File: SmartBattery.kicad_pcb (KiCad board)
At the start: 2 copper layers, 102 parts, among them J1 USB_C_Receptacle_USB2.0, J10 Conn_01x02, J11 Conn_01x02, J2 ST-USB-003A, J3 RJ45_LED_Shielded, J4 Conn_01x02, J5 Conn_01x02, J6 Conn_01x02, J7 Conn_01x02, J8 Conn_01x02, J9 Conn_01x02, Q1 2n7002K, Q2 AO4468, Q3 AO4468, Q4 AO4468, Q5 AO4468, Q6 2n7002K, SW1 SW_Push, SW2 SW_Push, U101 BQ2947xx, U102 BQ40Z50

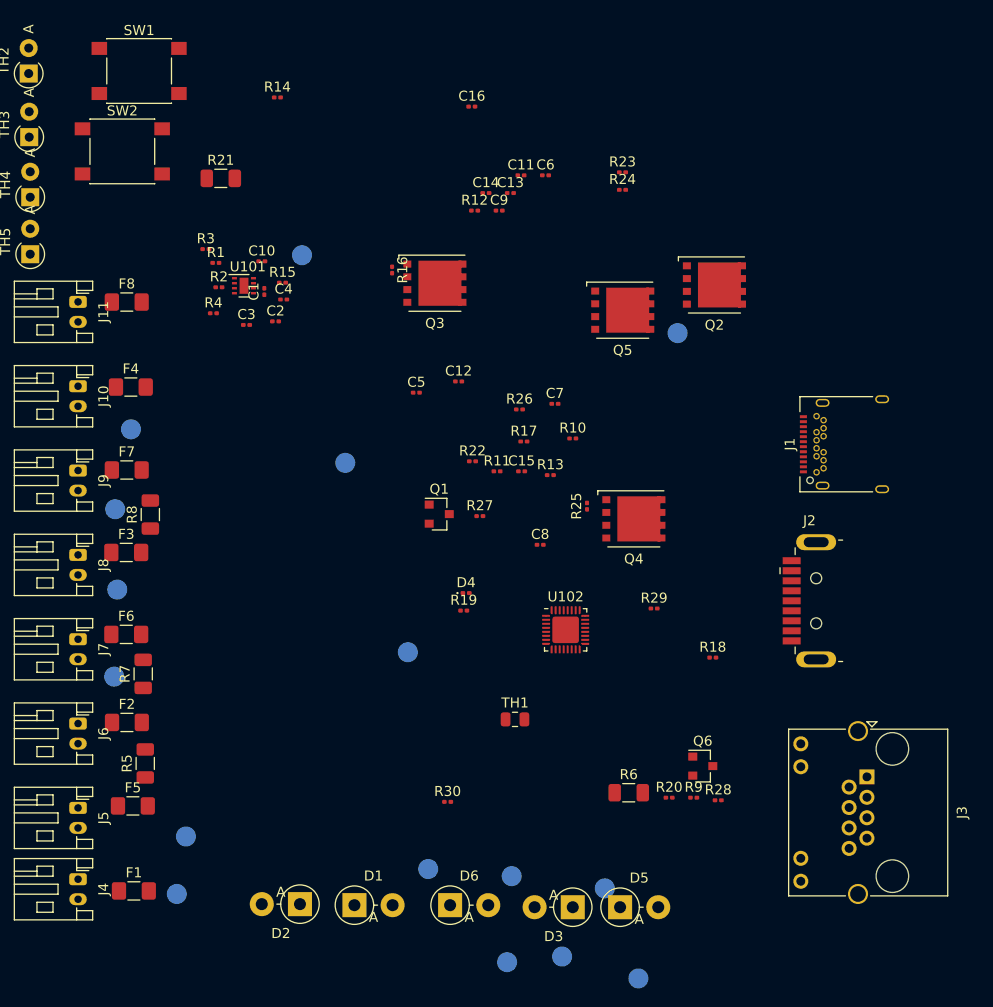
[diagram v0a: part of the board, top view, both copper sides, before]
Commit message: Added capacitors, inductors to charger page. Fixed capacitor sizes.
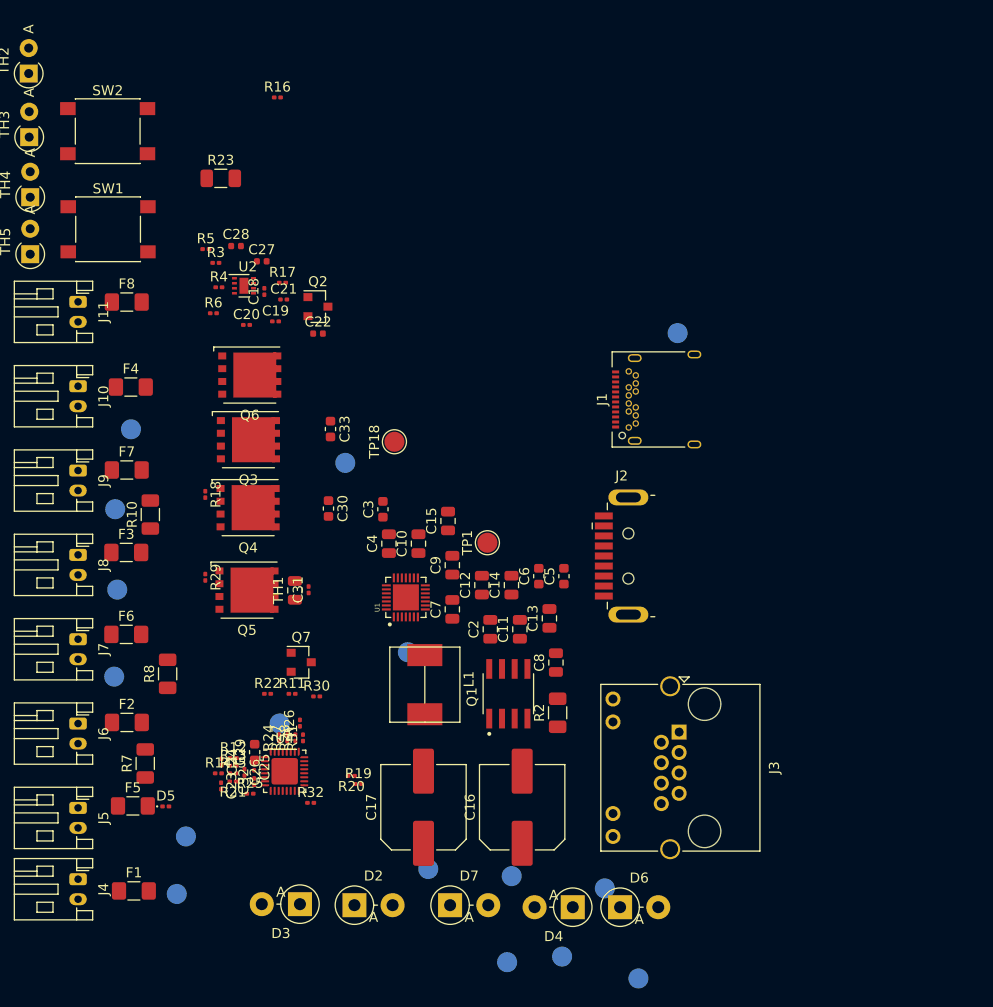
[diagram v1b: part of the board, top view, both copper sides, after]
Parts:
- removed the R7 at (66.0, 108.5)
- added C10: 10u, Capacitor_SMD:C_0805_2012Metric, F.Cu at (93.5, 95.5)
- added C11: 10u, Capacitor_SMD:C_0805_2012Metric, F.Cu at (103.6, 104.1)
- added C12: 22u, Capacitor_SMD:C_0805_2012Metric, F.Cu at (99.8, 99.7)
- added C13: 22u, Capacitor_SMD:C_0805_2012Metric, F.Cu at (106.5, 103.0)
- added C14: 22u, Capacitor_SMD:C_0805_2012Metric, F.Cu at (102.7, 99.7)
- added C15: 22u, Capacitor_SMD:C_0805_2012Metric, F.Cu at (96.4, 93.3)
- added C16: 220u, Capacitor_SMD:C_Elec_8x10.2, F.Cu at (103.8, 121.8)
- added C17: 220u, Capacitor_SMD:C_Elec_8x10.2, F.Cu at (94.0, 121.8)
- added C2: 10u, Capacitor_SMD:C_0805_2012Metric, F.Cu at (100.6, 104.1)
- added C3: 0.1u, Capacitor_SMD:C_0603_1608Metric, F.Cu at (89.9, 92.1)
- added C4: 22u, Capacitor_SMD:C_0805_2012Metric, F.Cu at (90.5, 95.5)
- added C5: 0.1u, Capacitor_SMD:C_0603_1608Metric, F.Cu at (108.0, 98.8)
- added C6: 0.1u, Capacitor_SMD:C_0603_1608Metric, F.Cu at (105.5, 98.8)
- added C7: 22u, Capacitor_SMD:C_0805_2012Metric, F.Cu at (96.8, 102.1)
- added C8: 10u, Capacitor_SMD:C_0805_2012Metric, F.Cu at (107.2, 107.4)
- added C9: 22u, Capacitor_SMD:C_0805_2012Metric, F.Cu at (96.8, 97.7)
- added L1: MWSA0603-2R2MT, SmartBattery:MWSA0603, F.Cu at (92.2, 111.5)
- added Q2: 2n7002K, Package_TO_SOT_SMD:SOT-23, F.Cu at (83.4, 71.9)
- added R2: 0.01, Resistor_SMD:R_1206_3216Metric, F.Cu at (107.4, 112.4)
- added TP1: TestPoint, TestPoint:TestPoint_Pad_D2.0mm, F.Cu at (100.3, 95.4)
- added TP18: TestPoint, TestPoint:TestPoint_Pad_D2.0mm, F.Cu at (91.1, 85.4)
- added U1: bq2477x, SmartBattery:QFN40P400X400X80-29N, F.Cu at (92.2, 100.9)
- C18: renamed from C1; value C -> 0.1u 6.3v
- C19: renamed from C2; value C -> 0.1u 6.3v
- C20: renamed from C3; value C -> 0.1u 6.3v
- C21: renamed from C4; value C -> 0.1u 6.3v
- C22: renamed from C5; value 0.1uF -> 0.1uF 25v; footprint Capacitor_SMD:C_0201_0603Metric -> Capacitor_SMD:C_0402_1005Metric
- C23: renamed from C6; value C -> 0.1u 6.3v
- C24: renamed from C7; value C -> 0.1u 6.3v
- C25: renamed from C8; value C -> 0.1u 6.3v
- C26: renamed from C9; value C -> 0.1u 6.3v
- C27: renamed from C10; value C -> 0.1u 20v; footprint Capacitor_SMD:C_0201_0603Metric -> Capacitor_SMD:C_0402_1005Metric
- C28: renamed from C11; value C -> 0.1u 20v; footprint Capacitor_SMD:C_0201_0603Metric -> Capacitor_SMD:C_0402_1005Metric
- C29: renamed from C12; value 2.2u -> 2.2u 50v; footprint Capacitor_SMD:C_0201_0603Metric -> Capacitor_SMD:C_0603_1608Metric
- C30: renamed from C13; footprint Capacitor_SMD:C_0201_0603Metric -> Capacitor_SMD:C_0603_1608Metric
- C32: renamed from C15; value 0.1u -> 0.1u 6.3v
- C33: renamed from C16; footprint Capacitor_SMD:C_0201_0603Metric -> Capacitor_SMD:C_0603_1608Metric
- Q1: value 2n7002K -> AO4407A; footprint Package_TO_SOT_SMD:SOT-23 -> SmartBattery:SOIC127P600X175-8N
- U2: renamed from U101; value BQ2947xx -> BQ294706DSGR
- moved R25 72.3 mm to (76.7, 120.5)
- moved C23 69.0 mm to (73.8, 119.7), turned to 270 degrees
- moved R26 62.2 mm to (81.6, 113.5), turned to 90 degrees
- moved R14 61.7 mm to (73.5, 118.5)
- moved C26 61.6 mm to (76.1, 118.4), turned to 270 degrees
- moved Q3 49.0 mm to (76.5, 85.2)
- moved C24 48.8 mm to (73.8, 117.3), turned to 270 degrees
- moved R8 47.5 mm to (68.4, 108.5), turned to 90 degrees
- moved TP13 46.8 mm to (79.6, 113.5)
- moved R12 46.5 mm to (75.0, 116.9)
- moved R15 43.5 mm to (75.0, 118.5)
- moved C31 43.4 mm to (82.5, 100.1), turned to 90 degrees
- moved C29 42.2 mm to (77.1, 116.3), turned to 90 degrees
- moved R22 41.4 mm to (78.4, 110.5)
- moved Q7 41.4 mm to (81.8, 107.4)
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- renumbered C14 to C31, D1 to D2, D2 to D3, D3 to D4, D4 to D5, D5 to D6, D6 to D7, Q2 to Q3, Q3 to Q4, Q4 to Q5, Q5 to Q6, Q6 to Q7, R8 to R10, R9 to R11, R10 to R12, R11 to R13, R12 to R14, R13 to R15, R14 to R16, R15 to R17, R16 to R18, R17 to R19, R18 to R20, R19 to R21, R20 to R22, R21 to R23, R22 to R24, R23 to R25, R24 to R26, R25 to R27, R26 to R28, R27 to R29, R1 to R3, R28 to R30, R29 to R31, R30 to R32, R2 to R4, R3 to R5, R4 to R6, R5 to R7, R6 to R8, TP17 to TP10, TP18 to TP11, TP19 to TP12, TP20 to TP13, TP21 to TP14, TP22 to TP15, TP23 to TP16, TP24 to TP17, TP9 to TP2, TP10 to TP3, TP11 to TP4, TP12 to TP5, TP13 to TP6, TP14 to TP7, TP15 to TP8, TP16 to TP9, U102 to U4
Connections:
- net BATT_SHUTDOWN renamed /Battery connection and protection/BATT_SHUTDOWN_N
- net BTP_INT renamed /Battery connection and protection/BATT_INT
- net PACK_+ renamed /Battery connection and protection/BATT_PACK_P
- net SMB_C renamed /Battery connection and protection/BATT_SMB_C
- net SMB_D renamed /Battery connection and protection/BATT_SMB_D
- Q1 pad 1: FUSE_HEATER -> Net-(C10-Pad1)
- Q1 pad 2: BAT_VN_0 -> Net-(C10-Pad1)
- Q1 pad 3: Net-(Q1-Pad3) -> Net-(C10-Pad1)
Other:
- net class Default: clearance 0.2 -> 0.18; trace_width 0.25 -> 0.18; via_dia 0.8 -> 0.4; via_drill 0.4 -> 0.3
- rule trace_clearance: 0.2 -> 0.18
- rule trace_min: 0.2 -> 0.16

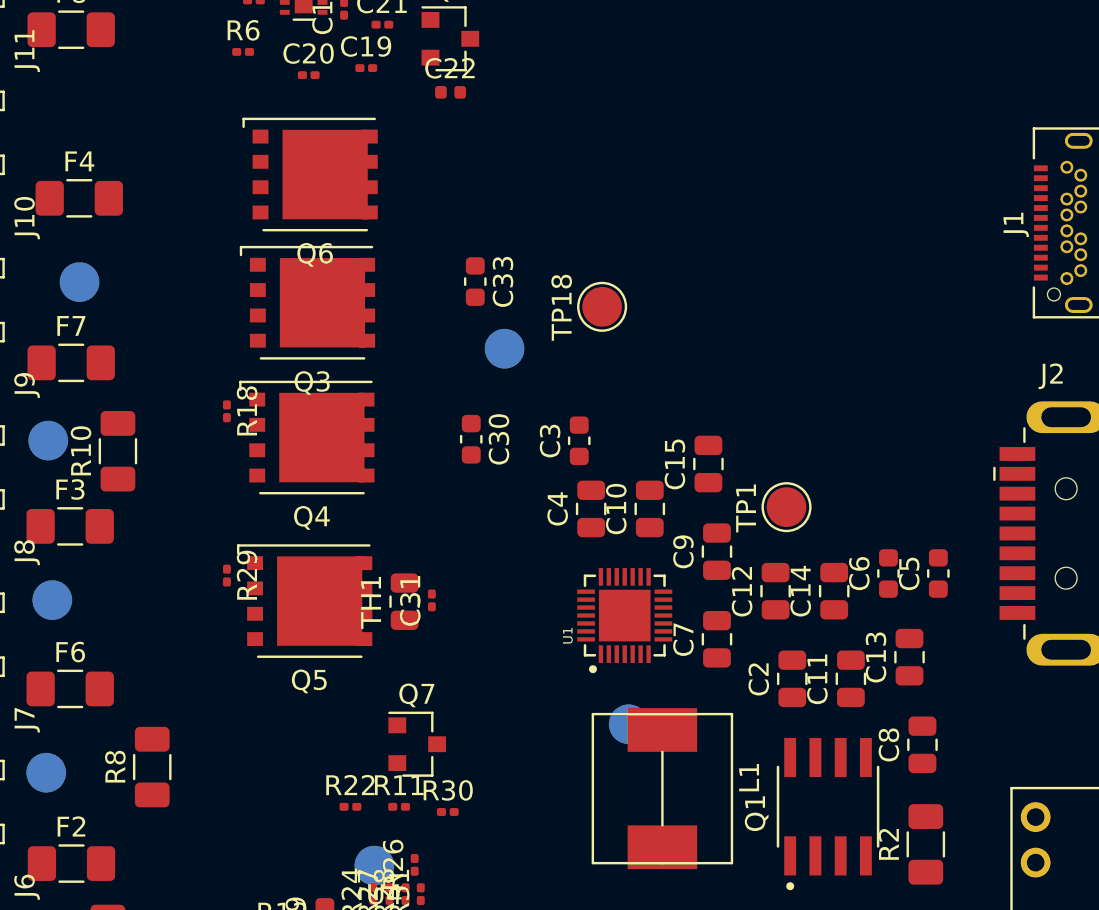
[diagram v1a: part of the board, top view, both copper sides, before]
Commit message: Added bunch of cap to charger, made footprint for diode + fuse
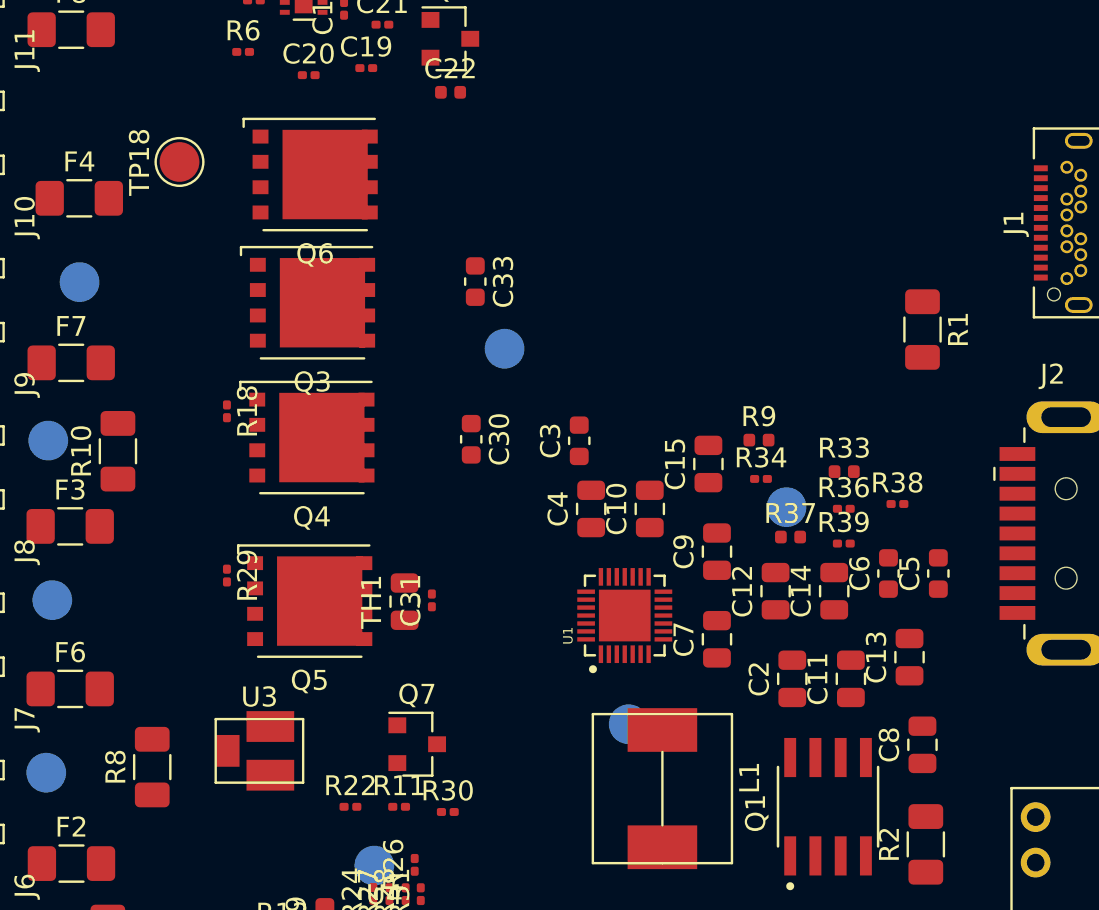
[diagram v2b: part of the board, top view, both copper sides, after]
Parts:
- added R1: 0.01, Resistor_SMD:R_1206_3216Metric, F.Cu at (107.2, 86.5)
- added R33: 2, Resistor_SMD:R_0402_1005Metric, F.Cu at (103.2, 93.7)
- added R34: 10M, Resistor_SMD:R_0201_0603Metric, F.Cu at (99.1, 94.0)
- added R36: 0, Resistor_SMD:R_0201_0603Metric, F.Cu at (103.2, 95.5)
- added R37: 15, Resistor_SMD:R_0402_1005Metric, F.Cu at (100.5, 97.0)
- added R38: 0, Resistor_SMD:R_0201_0603Metric, F.Cu at (105.9, 95.3)
- added R39: 1M, Resistor_SMD:R_0201_0603Metric, F.Cu at (103.2, 97.3)
- added R9: 10M, Resistor_SMD:R_0402_1005Metric, F.Cu at (99.0, 92.1)
- added U3: ITV4030, SmartBattery:ITV4030, F.Cu at (73.8, 107.7)
- TP1: moved to B.Cu
- moved TP18 22.5 mm to (69.8, 78.1)
- turned TP1 to 270 degrees
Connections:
- net Net-(U1-Pad7) renamed /Charger/IADP
- net Net-(U1-Pad8) renamed /Charger/IBAT
- U1 pad 22: Net-(U1-Pad22) -> GND
- U1 pad 29: Net-(U1-Pad29) -> GND
- U1 pad 9: Net-(U1-Pad9) -> /Charger/PMON

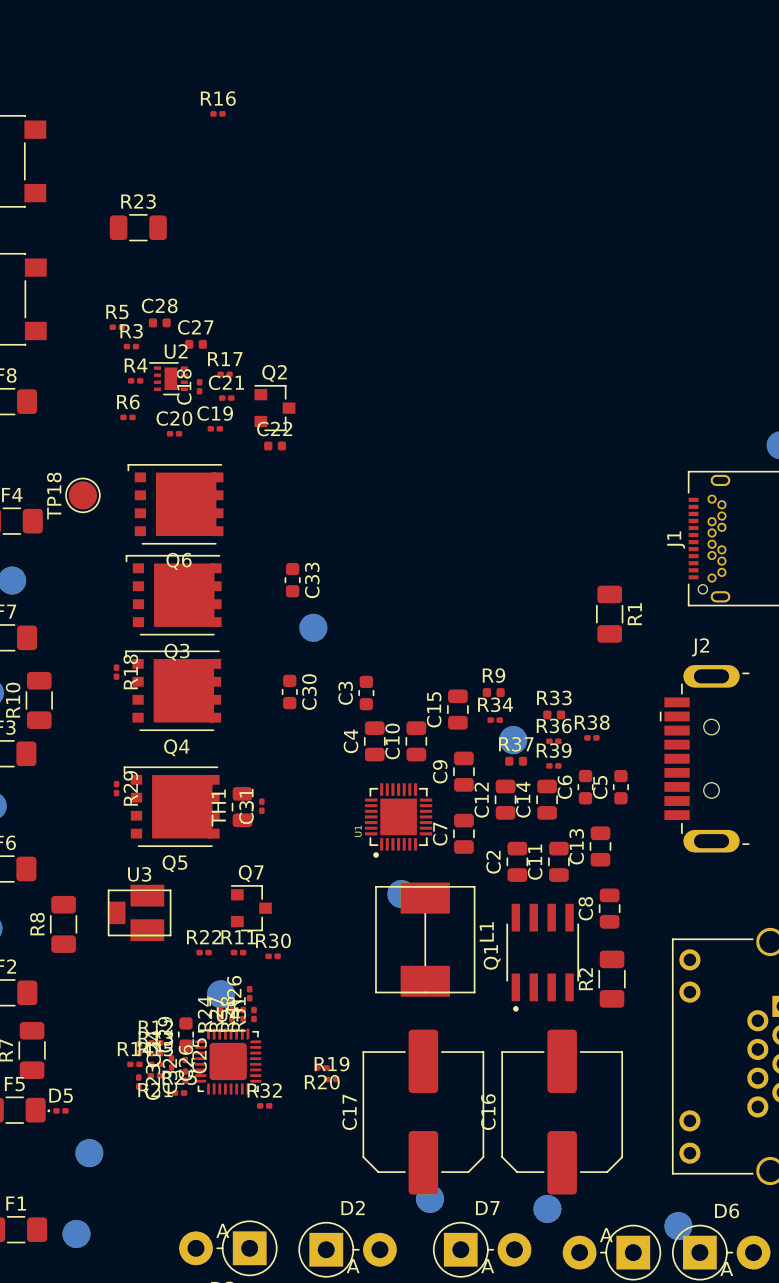
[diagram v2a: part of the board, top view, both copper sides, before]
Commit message: Finished Charger section, assigned all footprints. Next is output and then peripherals.
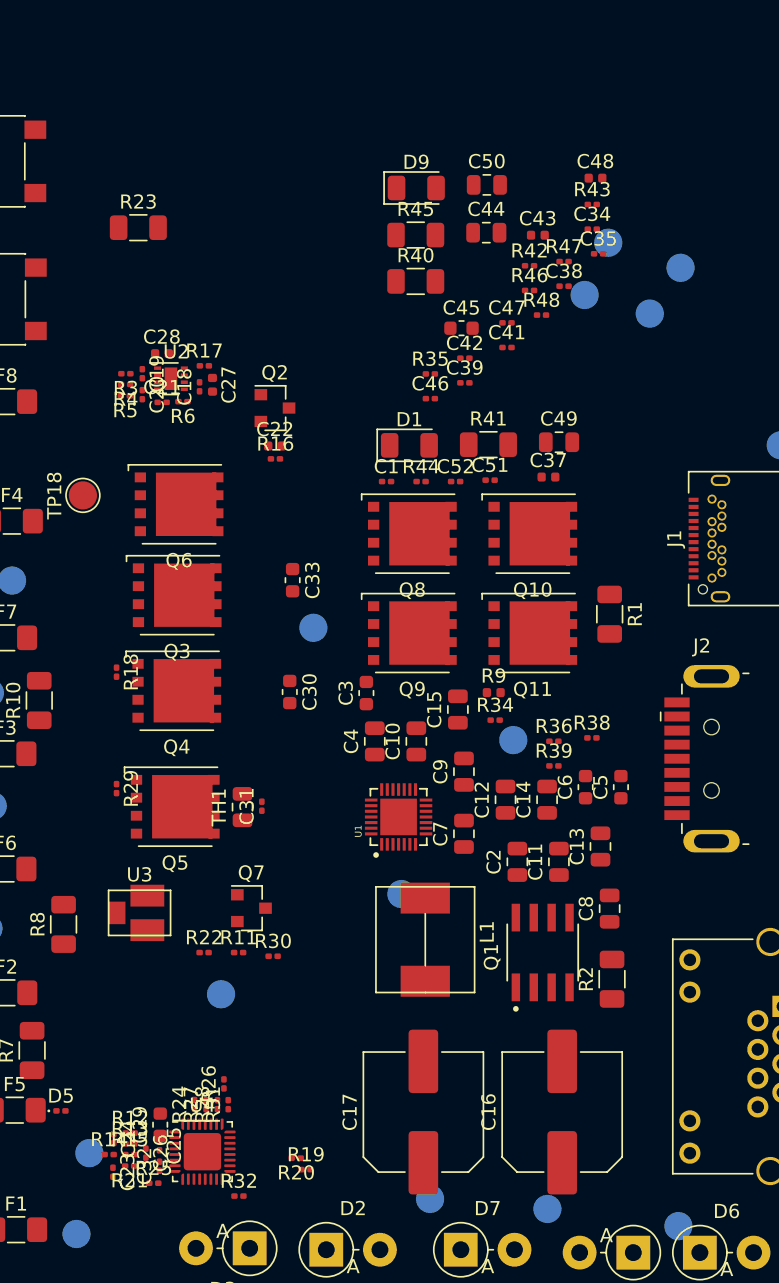
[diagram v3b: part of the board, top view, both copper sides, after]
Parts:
- removed R33: 2, Resistor_SMD:R_0402_1005Metric
- removed R37: 15, Resistor_SMD:R_0402_1005Metric
- added C1: 1uF 16v, Capacitor_SMD:C_0201_0603Metric, F.Cu at (91.4, 77.1)
- added C34: 1uF 16v, Capacitor_SMD:C_0201_0603Metric, F.Cu at (106.0, 59.2)
- added C35: 1uF 16v, Capacitor_SMD:C_0201_0603Metric, F.Cu at (106.4, 60.9)
- added C37: 1uF 25v, Capacitor_SMD:C_0402_1005Metric, F.Cu at (102.8, 76.8)
- added C38: 0.1uF 25v, Capacitor_SMD:C_0201_0603Metric, F.Cu at (104.0, 63.2)
- added C39: 0.1uF, Capacitor_SMD:C_0201_0603Metric, F.Cu at (96.9, 70.1)
- added C41: 0.1uF 25v, Capacitor_SMD:C_0201_0603Metric, F.Cu at (99.9, 67.6)
- added C42: 0.01uF, Capacitor_SMD:C_0201_0603Metric, F.Cu at (96.9, 68.3)
- added C43: 1uF 25v, Capacitor_SMD:C_0402_1005Metric, F.Cu at (102.1, 59.6)
- added C44: 22u, Capacitor_SMD:C_0805_2012Metric, F.Cu at (98.4, 59.4)
- added C45: 2.2uF 25v, Capacitor_SMD:C_0603_1608Metric, F.Cu at (96.7, 66.2)
- added C46: 2200pF, Capacitor_SMD:C_0201_0603Metric, F.Cu at (94.5, 71.2)
- added C47: 0.1uF, Capacitor_SMD:C_0201_0603Metric, F.Cu at (99.9, 65.8)
- added C48: 1uF 25v, Capacitor_SMD:C_0402_1005Metric, F.Cu at (106.2, 55.6)
- added C49: 10u, Capacitor_SMD:C_0805_2012Metric, F.Cu at (103.6, 74.3)
- added C50: 10u, Capacitor_SMD:C_0805_2012Metric, F.Cu at (98.5, 56.0)
- added C51: 47n, Capacitor_SMD:C_0201_0603Metric, F.Cu at (98.7, 77.0)
- added C52: 0.1uF 25v, Capacitor_SMD:C_0201_0603Metric, F.Cu at (96.3, 77.1)
- added D1: CD1206-S01575, Diode_SMD:D_1206_3216Metric, F.Cu at (93.0, 74.5)
- added D9: CD1206-S01575, Diode_SMD:D_1206_3216Metric, F.Cu at (93.5, 56.3)
- added Q10: AO4468, Package_TO_SOT_SMD:TDSON-8-1, F.Cu at (101.7, 80.8)
- added Q11: AO4468, Package_TO_SOT_SMD:TDSON-8-1, F.Cu at (101.7, 87.8)
- added Q8: AO4468, Package_TO_SOT_SMD:TDSON-8-1, F.Cu at (93.2, 80.8)
- added Q9: AO4468, Package_TO_SOT_SMD:TDSON-8-1, F.Cu at (93.2, 87.8)
- added R35: DNP, Resistor_SMD:R_0201_0603Metric, F.Cu at (94.5, 69.5)
- added R40: 430k, Resistor_SMD:R_1206_3216Metric, F.Cu at (93.4, 62.9)
- added R41: 100k, Resistor_SMD:R_1206_3216Metric, F.Cu at (98.6, 74.5)
- added R42: 4.7, Resistor_SMD:R_0201_0603Metric, F.Cu at (101.5, 61.8)
- added R43: 4.02k, Resistor_SMD:R_0201_0603Metric, F.Cu at (106.0, 57.4)
- added R44: 4.02k, Resistor_SMD:R_0201_0603Metric, F.Cu at (93.8, 77.1)
- added R45: 10, Resistor_SMD:R_1206_3216Metric, F.Cu at (93.4, 59.6)
- added R46: 0, Resistor_SMD:R_0201_0603Metric, F.Cu at (101.5, 63.5)
- added R47: 0, Resistor_SMD:R_0201_0603Metric, F.Cu at (104.0, 61.5)
- added R48: 4.7, Resistor_SMD:R_0201_0603Metric, F.Cu at (102.4, 65.3)
- added TP19: TestPoint, TestPoint:TestPoint_Pad_D2.0mm, B.Cu at (105.4, 63.9)
- added TP20: TestPoint, TestPoint:TestPoint_Pad_D2.0mm, B.Cu at (112.2, 61.9)
- added TP21: TestPoint, TestPoint:TestPoint_Pad_D2.0mm, B.Cu at (110.0, 65.2)
- added TP22: TestPoint, TestPoint:TestPoint_Pad_D2.0mm, B.Cu at (107.1, 60.1)
- moved R16 24.8 mm to (83.5, 75.5)
- moved C23 6.66 mm to (71.9, 126.1)
- moved C29 6.66 mm to (75.3, 122.7)
- moved R12 6.66 mm to (73.2, 123.3)
- moved R13 6.66 mm to (73.1, 124.1)
- moved R14 6.66 mm to (71.7, 124.9)
- moved R15 6.66 mm to (73.1, 124.9)
- moved R19 6.66 mm to (85.6, 125.9)
- moved R20 6.66 mm to (84.9, 125.1)
- moved R24 6.66 mm to (77.7, 121.3)
- moved R26 6.66 mm to (79.8, 119.9)
- moved U4 6.66 mm to (78.3, 124.7)
- moved C25 6.66 mm to (75.2, 124.2)
- moved C32 6.66 mm to (75.2, 125.7)
- moved C24 6.66 mm to (72.0, 123.7)
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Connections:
- net Net-(U1-Pad10) renamed /Charger/PROCHOT_N
- net Net-(U1-Pad11) renamed /Charger/CHARGER_SDA
- net Net-(U1-Pad12) renamed /Charger/CHARGER_SCL
- net Net-(U1-Pad5) renamed /Charger/ACOK
- L1 pad 2: Net-(L1-Pad2) -> Net-(C51-Pad1)
- U1 pad 18: Net-(U1-Pad18) -> Net-(Q1-Pad4)
- U1 pad 19: Net-(U1-Pad19) -> /Charger/VSYS
- U1 pad 20: Net-(U1-Pad20) -> Net-(C10-Pad1)
- U1 pad 24: Net-(U1-Pad24) -> /Charger/REGN
- U1 pad 27: Net-(U1-Pad27) -> Net-(C51-Pad1)
- U1 pad 28: (no net) -> Net-(R45-Pad1)
